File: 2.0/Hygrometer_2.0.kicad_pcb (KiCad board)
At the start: 2 copper layers, 89.9 x 52.3 mm, 60 parts, among them J1 POWER, J2 DHT11, Q1 Q_NPN_BEC, Q2 Q_NPN_BEC, SW1 WAKE UP, U1 74HC595, U2 ATtiny45V-10P, U3 74HC595

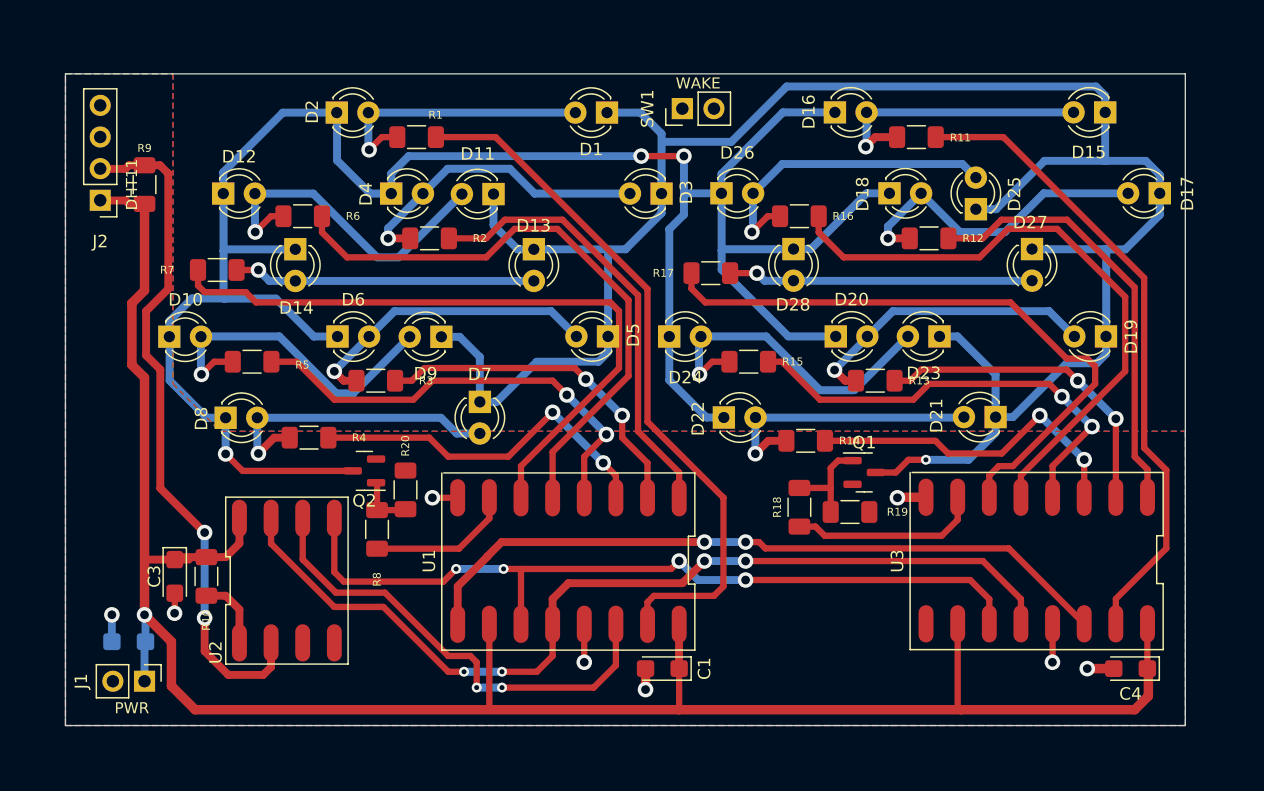
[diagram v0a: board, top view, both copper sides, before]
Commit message: Added button lines
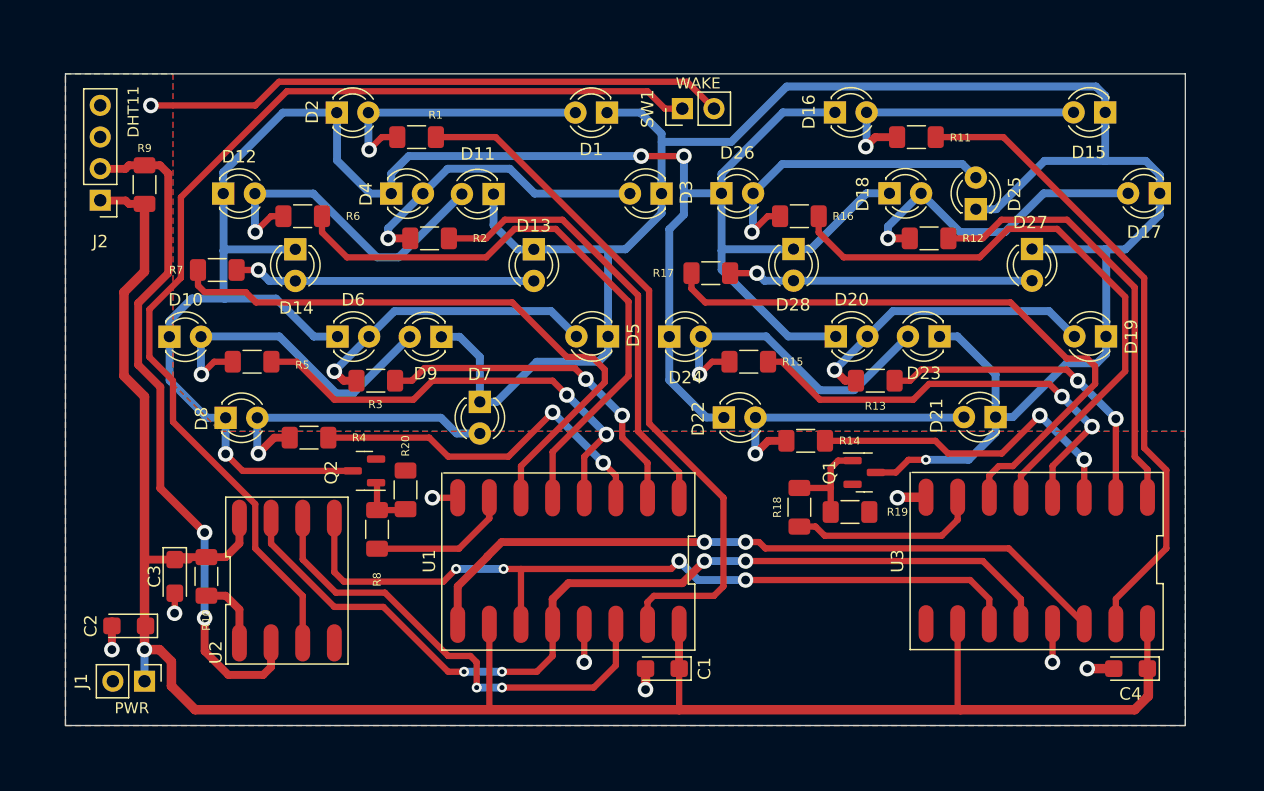
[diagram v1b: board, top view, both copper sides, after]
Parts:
- C2: moved to F.Cu
- moved C2 1.27 mm to (49.6, 72.0)
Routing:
- net Net-(SW1-Pad1): track 0.00 -> 86.3 mm
- net GND: track 18.2 -> 65.2 mm, vias 8 -> 9
- net Net-(R7-Pad2): track 54.2 -> 49.8 mm
- net VCC: track 166.5 -> 167.9 mm
- net Net-(J2-Pad2): track 55.2 -> 55.7 mm

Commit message: Updated resistors for LEDs
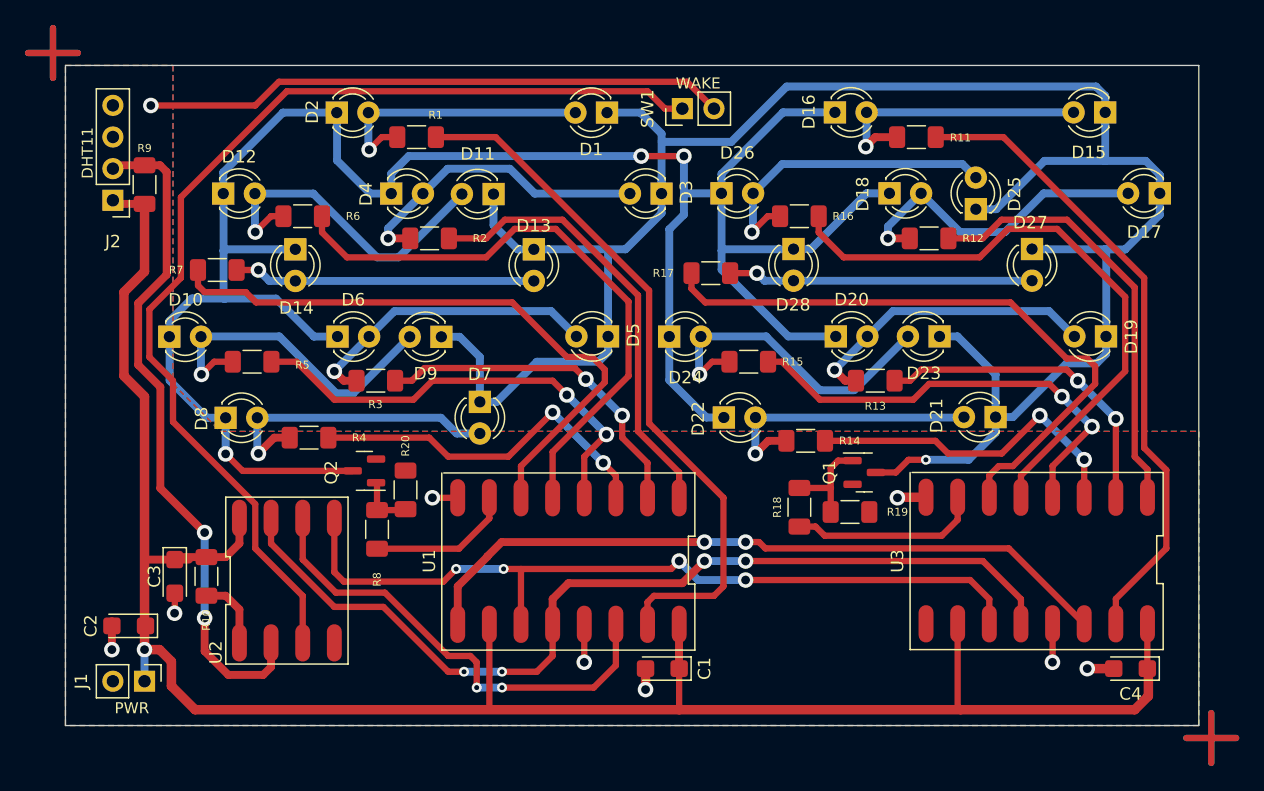
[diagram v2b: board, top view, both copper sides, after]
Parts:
- R1, R11, R12, R13, R14, R15, R16, R17, R2, R3, R4, R5, R6, R7: value 270 -> 100
- moved J2 1.02 mm to (48.4, 37.8)
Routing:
- net Net-(J2-Pad2): track 55.7 -> 54.6 mm
- net VCC: track 167.9 -> 166.9 mm
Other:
- board size 89.9 x 52.3 mm -> 91 x 53 mm
